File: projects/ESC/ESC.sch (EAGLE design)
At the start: 79 parts, among them J2 1755529, U1 STM32F405RGT6, U10 CSD88584Q5DCT, U11 CSD88584Q5DCT, U12 CSD88584Q5DCT, U13 CSD88584Q5DCT, U2 CSD88584Q5DCT, U3 CSD88584Q5DCT, U4 CSD88584Q5DCT, U5 CSD88584Q5DCT, U6 CSD88584Q5DCT, U7 CSD88584Q5DCT, U8 CSD88584Q5DCT, U9 CSD88584Q5DCT, Y1 ABLS2-4.096MHZ-D4Y-T

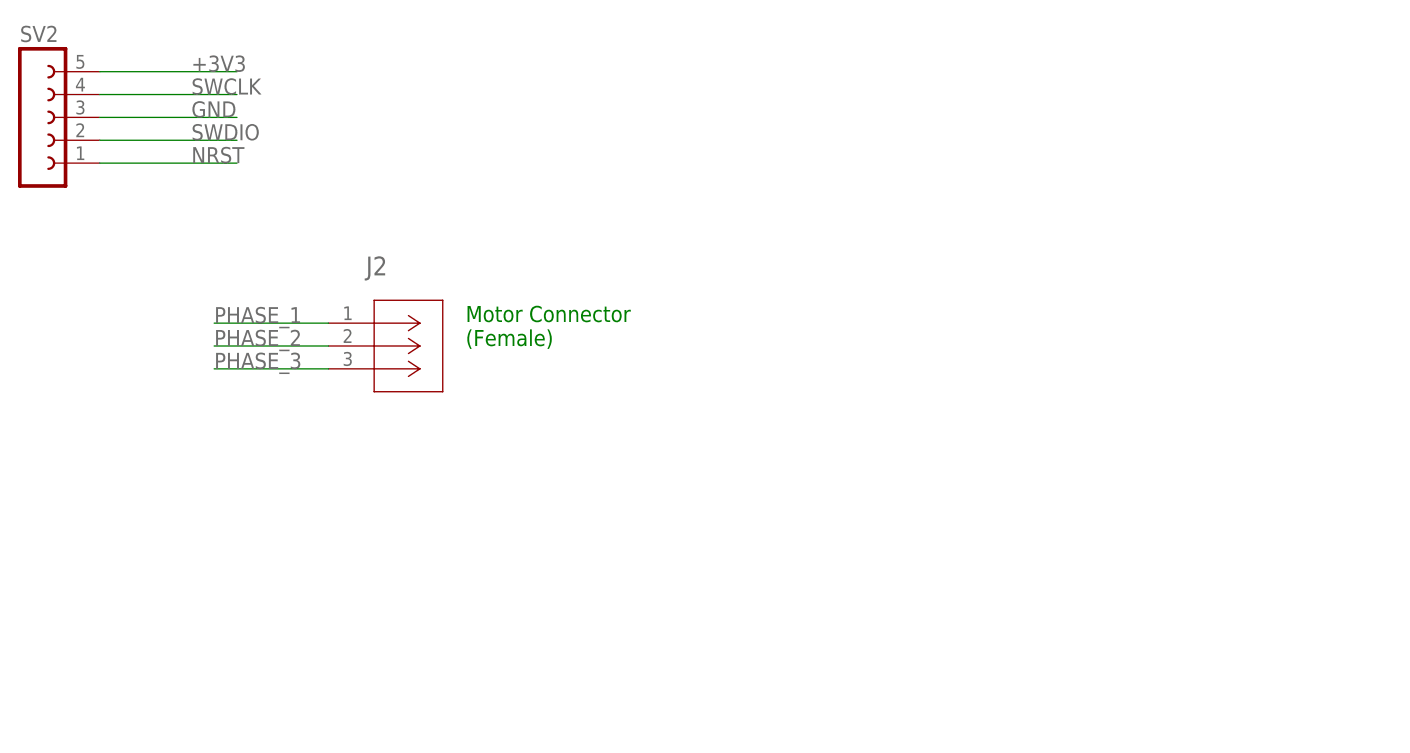
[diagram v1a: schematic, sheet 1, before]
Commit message: added motor 4 to mcu, etc.
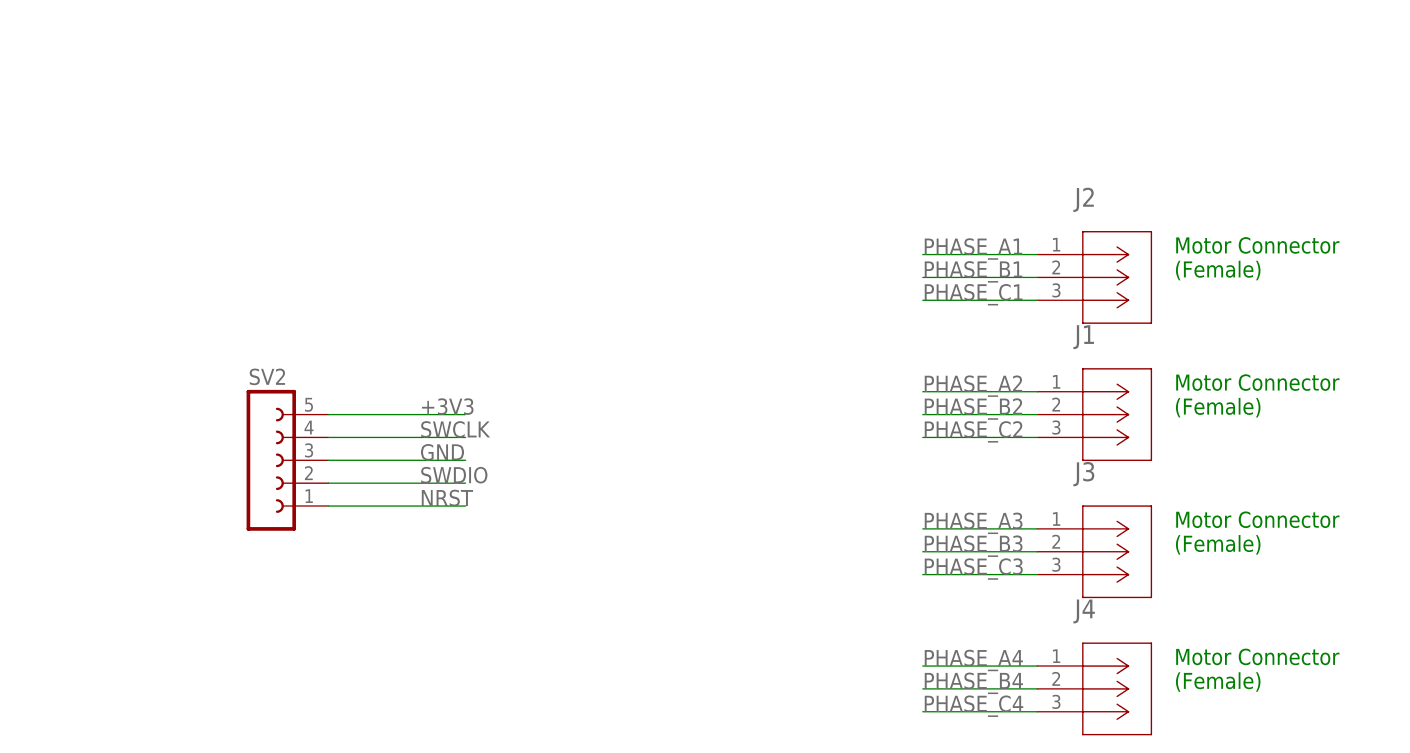
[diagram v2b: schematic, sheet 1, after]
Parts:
- added J1, J3, J4: 1755529, VESC_SHIT:1755529
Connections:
- removed net PHASE_1: J2.1
- removed net PHASE_2: J2.2
- removed net PHASE_3: J2.3
- new net FAULT_4: U1.PB2
- new net INHA_4: U1.PB7
- new net INHB_4: U1.PB6
- new net INHC_4: U1.PB5
- net EN_4: now also U1.PB1
- net INL_4: now also U1.PB4
- net PHASE_A1: now also J2.1
- net PHASE_A2: now also J1.1
- net PHASE_A3: now also J3.1
- net PHASE_A4: now also J4.1
- net PHASE_B1: now also J2.2
- net PHASE_B2: now also J1.2
- net PHASE_B3: now also J3.2
- net PHASE_B4: now also J4.2
- net PHASE_C1: now also J2.3
- net PHASE_C2: now also J1.3
- net PHASE_C3: now also J3.3
- net PHASE_C4: now also J4.3
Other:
- moved on the sheet: J2, SV2
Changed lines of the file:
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@@
 <part name="GND29" library="SparkFun-PowerSymbols" library_urn="urn:adsk.eagle:library:530" deviceset="GND" device=""/>
 <part name="GND30" library="SparkFun-PowerSymbols" library_urn="urn:adsk.eagle:library:530" deviceset="GND" device=""/>
+<part name="J1" library="VESC_SHIT" deviceset="1755529" device=""/>
+<part name="J3" library="VESC_SHIT" deviceset="1755529" device=""/>
+<part name="J4" library="VESC_SHIT" deviceset="1755529" device=""/>
 </parts>
 <sheets>
@@
 <description>Connectors</description>
 <plain>
-<text x="137.16" y="83.82" size="1.778" layer="91">Motor Connector
+<text x="215.9" y="91.44" size="1.778" layer="91">Motor Connector
+(Female)</text>
+<text x="215.9" y="76.2" size="1.778" layer="91">Motor Connector
+(Female)</text>
+<text x="215.9" y="60.96" size="1.778" layer="91">Motor Connector
+(Female)</text>
+<text x="215.9" y="45.72" size="1.778" layer="91">Motor Connector
 (Female)</text>
 </plain>
@@
 <attribute name="LAST_DATE_TIME" x="217.17" y="10.16" size="2.286" layer="94"/>
 </instance>
-<instance part="J2" gate="A" x="121.92" y="86.36" smashed="yes">
-<attribute name="NAME" x="126.0856" y="91.6686" size="2.0828" layer="95" ratio="6" rot="SR0"/>
-</instance>
-<instance part="SV2" gate="G$1" x="88.9" y="109.22" smashed="yes">
-<attribute name="VALUE" x="87.63" y="99.06" size="1.778" layer="96"/>
-<attribute name="NAME" x="87.63" y="117.602" size="1.778" layer="95"/>
+<instance part="J2" gate="A" x="200.66" y="93.98" smashed="yes">
+<attribute name="NAME" x="204.8256" y="99.2886" size="2.0828" layer="95" ratio="6" rot="SR0"/>
+</instance>
+<instance part="SV2" gate="G$1" x="114.3" y="71.12" smashed="yes">
+<attribute name="VALUE" x="113.03" y="60.96" size="1.778" layer="96"/>
+<attribute name="NAME" x="113.03" y="79.502" size="1.778" layer="95"/>
+</instance>
+<instance part="J1" gate="A" x="200.66" y="78.74" smashed="yes">
+<attribute name="NAME" x="204.8256" y="84.0486" size="2.0828" layer="95" ratio="6" rot="SR0"/>
+</instance>
+<instance part="J3" gate="A" x="200.66" y="63.5" smashed="yes">
+<attribute name="NAME" x="204.8256" y="68.8086" size="2.0828" layer="95" ratio="6" rot="SR0"/>
+</instance>
+<instance part="J4" gate="A" x="200.66" y="48.26" smashed="yes">
+<attribute name="NAME" x="204.8256" y="53.5686" size="2.0828" layer="95" ratio="6" rot="SR0"/>
 </instance>
 </instances>
@@
 </busses>
 <nets>
-<net name="PHASE_1" class="0">
+<net name="PHASE_A4" class="0">
+<segment>
+<pinref part="J4" gate="A" pin="1"/>
+<wire x1="200.66" y1="48.26" x2="187.96" y2="48.26" width="0.1524" layer="91"/>
+<label x="187.96" y="48.26" size="1.778" layer="95"/>
+</segment>
+</net>
+<net name="PHASE_B4" class="0">
+<segment>
+<pinref part="J4" gate="A" pin="2"/>
+<wire x1="200.66" y1="45.72" x2="187.96" y2="45.72" width="0.1524" layer="91"/>
+<label x="187.96" y="45.72" size="1.778" layer="95"/>
+</segment>
+</net>
+<net name="PHASE_C4" class="0">
+<segment>
+<pinref part="J4" gate="A" pin="3"/>
+<wire x1="200.66" y1="43.18" x2="187.96" y2="43.18" width="0.1524" layer="91"/>
+<label x="187.96" y="43.18" size="1.778" layer="95"/>
+</segment>
+</net>
+<net name="GND" class="0">
+<segment>
+<pinref part="SV2" gate="G$1" pin="3"/>
+<wire x1="121.92" y1="71.12" x2="137.16" y2="71.12" width="0.1524" layer="91"/>
+<label x="132.08" y="71.12" size="1.778" layer="95"/>
+</segment>
+</net>
+<net name="+3V3" class="0">
+<segment>
+<pinref part="SV2" gate="G$1" pin="5"/>
+<wire x1="121.92" y1="76.2" x2="137.16" y2="76.2" width="0.1524" layer="91"/>
+<label x="132.08" y="76.2" size="1.778" layer="95"/>
+</segment>
+</net>
+<net name="NRST" class="0">
+<segment>
+<pinref part="SV2" gate="G$1" pin="1"/>
+<wire x1="121.92" y1="66.04" x2="137.16" y2="66.04" width="0.1524" layer="91"/>
+<label x="132.08" y="66.04" size="1.778" layer="95"/>
+</segment>
+</net>
+<net name="SWDIO" class="0">
+<segment>
+<pinref part="SV2" gate="G$1" pin="2"/>
+<wire x1="121.92" y1="68.58" x2="137.16" y2="68.58" width="0.1524" layer="91"/>
+<label x="132.08" y="68.58" size="1.778" layer="95"/>
+</segment>
+</net>
+<net name="SWCLK" class="0">
+<segment>
+<pinref part="SV2" gate="G$1" pin="4"/>
+<wire x1="121.92" y1="73.66" x2="137.16" y2="73.66" width="0.1524" layer="91"/>
+<label x="132.08" y="73.66" size="1.778" layer="95"/>
+</segment>
+</net>
+<net name="PHASE_A1" class="0">
 <segment>
 <pinref part="J2" gate="A" pin="1"/>
-<wire x1="121.92" y1="86.36" x2="109.22" y2="86.36" width="0.1524" layer="91"/>
-<label x="109.22" y="86.36" size="1.778" layer="95"/>
-</segment>
-</net>
-<net name="PHASE_2" class="0">
+<wire x1="200.66" y1="93.98" x2="187.96" y2="93.98" width="0.1524" layer="91"/>
+<label x="187.96" y="93.98" size="1.778" layer="95"/>
+</segment>
+</net>
+<net name="PHASE_B1" class="0">
 <segment>
 <pinref part="J2" gate="A" pin="2"/>
-<wire x1="121.92" y1="83.82" x2="109.22" y2="83.82" width="0.1524" layer="91"/>
-<label x="109.22" y="83.82" size="1.778" layer="95"/>
-</segment>
-</net>
-<net name="PHASE_3" class="0">
+<wire x1="200.66" y1="91.44" x2="187.96" y2="91.44" width="0.1524" layer="91"/>
+<label x="187.96" y="91.44" size="1.778" layer="95"/>
+</segment>
+</net>
+<net name="PHASE_C1" class="0">
 <segment>
 <pinref part="J2" gate="A" pin="3"/>
-<wire x1="121.92" y1="81.28" x2="109.22" y2="81.28" width="0.1524" layer="91"/>
-<label x="109.22" y="81.28" size="1.778" layer="95"/>
-</segment>
-</net>
-<net name="GND" class="0">
-<segment>
-<pinref part="SV2" gate="G$1" pin="3"/>
-<wire x1="96.52" y1="109.22" x2="111.76" y2="109.22" width="0.1524" layer="91"/>
-<label x="106.68" y="109.22" size="1.778" layer="95"/>
-</segment>
-</net>
-<net name="+3V3" class="0">
-<segment>
-<pinref part="SV2" gate="G$1" pin="5"/>
-<wire x1="96.52" y1="114.3" x2="111.76" y2="114.3" width="0.1524" layer="91"/>
-<label x="106.68" y="114.3" size="1.778" layer="95"/>
-</segment>
-</net>
-<net name="NRST" class="0">
-<segment>
-<pinref part="SV2" gate="G$1" pin="1"/>
-<wire x1="96.52" y1="104.14" x2="111.76" y2="104.14" width="0.1524" layer="91"/>
-<label x="106.68" y="104.14" size="1.778" layer="95"/>
-</segment>
-</net>
-<net name="SWDIO" class="0">
-<segment>
-<pinref part="SV2" gate="G$1" pin="2"/>
-<wire x1="96.52" y1="106.68" x2="111.76" y2="106.68" width="0.1524" layer="91"/>
-<label x="106.68" y="106.68" size="1.778" layer="95"/>
-</segment>
-</net>
-<net name="SWCLK" class="0">
-<segment>
-<pinref part="SV2" gate="G$1" pin="4"/>
-<wire x1="96.52" y1="111.76" x2="111.76" y2="111.76" width="0.1524" layer="91"/>
-<label x="106.68" y="111.76" size="1.778" layer="95"/>
+<wire x1="200.66" y1="88.9" x2="187.96" y2="88.9" width="0.1524" layer="91"/>
+<label x="187.96" y="88.9" size="1.778" layer="95"/>
+</segment>
+</net>
+<net name="PHASE_A2" class="0">
+<segment>
+<pinref part="J1" gate="A" pin="1"/>
+<wire x1="200.66" y1="78.74" x2="187.96" y2="78.74" width="0.1524" layer="91"/>
+<label x="187.96" y="78.74" size="1.778" layer="95"/>
+</segment>
+</net>
+<net name="PHASE_B2" class="0">
+<segment>
+<pinref part="J1" gate="A" pin="2"/>
+<wire x1="200.66" y1="76.2" x2="187.96" y2="76.2" width="0.1524" layer="91"/>
+<label x="187.96" y="76.2" size="1.778" layer="95"/>
+</segment>
+</net>
+<net name="PHASE_C2" class="0">
+<segment>
+<pinref part="J1" gate="A" pin="3"/>
+<wire x1="200.66" y1="73.66" x2="187.96" y2="73.66" width="0.1524" layer="91"/>
+<label x="187.96" y="73.66" size="1.778" layer="95"/>
+</segment>
+</net>
+<net name="PHASE_A3" class="0">
+<segment>
+<pinref part="J3" gate="A" pin="1"/>
+<wire x1="200.66" y1="63.5" x2="187.96" y2="63.5" width="0.1524" layer="91"/>
+<label x="187.96" y="63.5" size="1.778" layer="95"/>
+</segment>
+</net>
+<net name="PHASE_B3" class="0">
+<segment>
+<pinref part="J3" gate="A" pin="2"/>
+<wire x1="200.66" y1="60.96" x2="187.96" y2="60.96" width="0.1524" layer="91"/>
+<label x="187.96" y="60.96" size="1.778" layer="95"/>
+</segment>
+</net>
+<net name="PHASE_C3" class="0">
+<segment>
+<pinref part="J3" gate="A" pin="3"/>
+<wire x1="200.66" y1="58.42" x2="187.96" y2="58.42" width="0.1524" layer="91"/>
+<label x="187.96" y="58.42" size="1.778" layer="95"/>
 </segment>
 </net>
@@
 </segment>
 </net>
+<net name="INHA_4" class="0">
+<segment>
+<pinref part="U1" gate="A" pin="PB7"/>
+<wire x1="160.02" y1="109.22" x2="170.18" y2="109.22" width="0.1524" layer="91"/>
+<label x="162.56" y="109.22" size="1.778" layer="95"/>
+</segment>
+</net>
+<net name="INHB_4" class="0">
+<segment>
+<pinref part="U1" gate="A" pin="PB6"/>
+<wire x1="160.02" y1="106.68" x2="170.18" y2="106.68" width="0.1524" layer="91"/>
+<label x="162.56" y="106.68" size="1.778" layer="95"/>
+</segment>
+</net>
+<net name="INHC_4" class="0">
+<segment>
+<pinref part="U1" gate="A" pin="PB5"/>
+<wire x1="160.02" y1="104.14" x2="170.18" y2="104.14" width="0.1524" layer="91"/>
+<label x="162.56" y="104.14" size="1.778" layer="95"/>
+</segment>
+</net>
+<net name="INL_4" class="0">
+<segment>
+<pinref part="U1" gate="A" pin="PB4"/>
+<wire x1="160.02" y1="101.6" x2="170.18" y2="101.6" width="0.1524" layer="91"/>
+<label x="162.56" y="101.6" size="1.778" layer="95"/>
+</segment>
+</net>
+<net name="EN_4" class="0">
+<segment>
+<pinref part="U1" gate="A" pin="PB1"/>
+<wire x1="114.3" y1="55.88" x2="104.14" y2="55.88" width="0.1524" layer="91"/>
+<wire x1="101.6" y1="55.88" x2="104.14" y2="55.88" width="0.1524" layer="91"/>
+<label x="101.6" y="55.88" size="1.778" layer="95"/>
+</segment>
+</net>
+<net name="FAULT_4" class="0">
+<segment>
+<pinref part="U1" gate="A" pin="PB2"/>
+<wire x1="114.3" y1="53.34" x2="101.6" y2="53.34" width="0.1524" layer="91"/>
+<label x="101.6" y="53.34" size="1.778" layer="95"/>
+</segment>
+</net>

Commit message: layout of one esc
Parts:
- removed C6, C7, C8, C9: 2.2uF, SparkFun-Capacitors:2.2UF-0603-10V-20%
- removed R12, R6: 1k, SparkFun-Resistors:1KOHM-0603-1/10W-1%
- removed U$8: TCAN337D, PI_Shield_Library:TCAN337D
- added C30, C32, C33, C34, C35, C38, C39, C40, C41: 4.7uF, SparkFun-Capacitors:4.7UF0603
- added C31: 0.1uF, SparkFun-Capacitors:0.1UF-0603-25V-(+80/-20%)
- added R28, R29: 60, SparkFun-Resistors:1KOHM-0603-1/10W-1%
- added RESET1: SWITCH, DiscreteComponents:SWITCH
- added SV1: (no value), con-lsta:FE05-1
- added U$5, U$7: SAMTEC, VESC_SHIT:SAMTEC
- added U$6: TCAN337D, PI_Shield_Library:TCAN337D
- C10, C11, C4, C5: value 2.2uF -> 4.7uF; device SparkFun-Capacitors:2.2UF-0603-10V-20% -> SparkFun-Capacitors:4.7UF0603
- C16, C2: value 0.1uF -> 4.7uF; device SparkFun-Capacitors:0.1UF-0603-25V-(+80/-20%) -> SparkFun-Capacitors:4.7UF0603
- Y1: value ABLS2-4.096MHZ-D4Y-T -> ECS-80-S-4X; device VESC_SHIT:ABLS2-4.096MHZ-D4Y-T -> ECS-80-S-4X:ECS-80-S-4X
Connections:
- net N$33 renamed IDRIVE
- net N$36 renamed VDS
- net PHASE_A2 renamed N$15
- removed net AIN: R4.1, R5.2, U1.PC2
- removed net DVDD_2: C23.1, R19.2, R21.2, U$1G$2.DVDD
- removed net N$12: U$1G$1.INHA
- removed net N$13: U$1G$1.INHB
- removed net N$15 (its old number): C16.2, R12.2, R6.1
- removed net N$29: U$1G$1.INHC
- new net N$46: C31.2, R28.1, R29.2
- new net OSC_IN: R5.2, U1.PD0_OSC_IN
- new net OSC_OUT: R3.2, U1.PD1_OSC_OUT
- net +3V3: now also C16.1, C30.1, C32.1, C33.1, C34.1, C35.1, C38.1, C39.1, C4.1, C40.1, C41.1, C5.1, R4.2, SV1.5, U$6.VCC; no longer U$8.VCC
- net 12V: now also C23.1, R10.2, R19.2, R21.2, R8.2, U$1G$2.DVDD, U$5G$2.1, U$5G$2.10, U$5G$2.11, U$5G$2.12, U$5G$2.13, U$5G$2.14, U$5G$2.15, U$5G$2.16, U$5G$2.17, U$5G$2.18, U$5G$2.19, U$5G$2.2, U$5G$2.20, U$5G$2.21, U$5G$2.22, U$5G$2.23, U$5G$2.24, U$5G$2.25, U$5G$2.26, U$5G$2.27, U$5G$2.28, U$5G$2.29, U$5G$2.3, U$5G$2.30, U$5G$2.31, U$5G$2.32, U$5G$2.4, U$5G$2.5, U$5G$2.6, U$5G$2.7, U$5G$2.8, U$5G$2.9; no longer R4.2
- net 3V3: now also U$5G$1.1, U$5G$1.10, U$5G$1.11, U$5G$1.12, U$5G$1.13, U$5G$1.14, U$5G$1.15, U$5G$1.16, U$5G$1.17, U$5G$1.18, U$5G$1.19, U$5G$1.2, U$5G$1.20, U$5G$1.21, U$5G$1.22, U$5G$1.23, U$5G$1.24, U$5G$1.3, U$5G$1.4, U$5G$1.5, U$5G$1.6, U$5G$1.7, U$5G$1.8, U$5G$1.9; no longer C4.1, C5.2, C6.1, C7.2, C8.1, C9.2, R3.2
- net CAN_H: now also R28.2, U$6.CANH, U$7G$1.24; no longer R6.2, U$8.CANH
- net CAN_L: now also R29.1, U$6.CANL, U$7G$1.23; no longer R12.1, U$8.CANL
- net CAN_RX: now also U$6.RXD; no longer U$8.RXD
- net CAN_TX: now also U$6.TXD; no longer U$8.TXD
- net DVDD_1: no longer R10.2, R8.2
- net GND: now also C10.2, C11.2, C16.2, C30.2, C31.1, C32.2, C33.2, C34.2, C35.2, C38.2, C39.2, C40.2, C41.2, C5.2, RESET1.P$1, SV1.3, U$6.GND, U$7G$2.1, U$7G$2.10, U$7G$2.11, U$7G$2.12, U$7G$2.13, U$7G$2.14, U$7G$2.15, U$7G$2.16, U$7G$2.17, U$7G$2.18, U$7G$2.19, U$7G$2.2, U$7G$2.20, U$7G$2.21, U$7G$2.22, U$7G$2.23, U$7G$2.24, U$7G$2.25, U$7G$2.26, U$7G$2.27, U$7G$2.28, U$7G$2.29, U$7G$2.3, U$7G$2.30, U$7G$2.31, U$7G$2.32, U$7G$2.4, U$7G$2.5, U$7G$2.6, U$7G$2.7, U$7G$2.8, U$7G$2.9; no longer C10.1, C11.1, C16.1, C5.1, C6.2, C7.1, C8.2, C9.1, R5.1, U$8.GND
- net INHA_2: now also U$1G$1.INHA
- net INHB_2: now also U$1G$1.INHB
- net INHC_3: now also U$1G$1.INHC
- net INL_1: no longer U1.PC8
- net INL_2: now also U1.PC8
- net N$7: now also C11.1, R3.1; no longer C10.2, U1.PD0_OSC_IN
- net N$8: now also C2.1, R5.1; no longer C11.2, U1.PD1_OSC_OUT
- net NRST: now also C10.1, R4.1, RESET1.P$2, SV1.1; no longer C2.1, R3.1
- net SWCLK: now also SV1.4
- net SWDIO: now also SV1.2
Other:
- note added: "Pin 1 (VBAT)"
- note added: "Pin 13 (VDDA)"
- note added: "Pin 19 (VDD_4)"
- note added: "Pin 32 (VDD_1)"
- note added: "Pin 48 (VDD_2)"
- note added: "Pin 64 (VDD_3)"
- note removed: "Caps + crystal should be as close as possible"
